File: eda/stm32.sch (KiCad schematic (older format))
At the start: 28 parts

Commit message: refs #41563 refined em-lock schematics, 2 spi rc522 devices added.
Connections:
- net labels added: PB13_SPI2_SCK, PB14_SPI2_MISO, PB15_SPI2_MOSI, PB5_RC522A_CS, PB6_RC522B_CS, PB7_RC522_RST, PB8_RC522A_IRQ, PB9_RC522B_IRQ
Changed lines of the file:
@@
 Connection ~ 11950 4450
 Connection ~ 12350 4450
+Text HLabel 9350 3800 0    60   Input ~ 0
+PB13_SPI2_SCK
+Text HLabel 9350 3900 0    60   Input ~ 0
+PB14_SPI2_MISO
+Text HLabel 9350 4000 0    60   Input ~ 0
+PB15_SPI2_MOSI
+Text HLabel 9350 3300 0    60   Input ~ 0
+PB8_RC522A_IRQ
+Text HLabel 9350 3400 0    60   Input ~ 0
+PB9_RC522B_IRQ
+Text HLabel 9350 3200 0    60   Input ~ 0
+PB7_RC522_RST
+Text HLabel 9350 3000 0    60   Input ~ 0
+PB5_RC522A_CS
+Text HLabel 9350 3100 0    60   Input ~ 0
+PB6_RC522B_CS
 $EndSCHEMATC

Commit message: refs #41563 fix stable schematics version
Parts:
- added R29: 0, I20:R_0805, symbol R
- C10, C11, C12, C13, C14, C15, C16, C17, C18, C19, C20, C9: renamed from C?; footprint I20:C_0805_HandSoldering -> I20:C_0805
- D4: renamed from D?; footprint I20:Fuse_SMD1206_Wave -> Diodes_ThroughHole:Diode_DO-201AD_Horizontal_RM15
- SW1: renamed from SW?; footprint I20:SW_SPST_B3U-1000P -> I20:smd_push
- gave numbers to parts that had none: 14
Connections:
- wire segments 74 -> 72
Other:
- moved on the sheet: C11, C12, CON1, D4, F1, P12, P8, P9, U2

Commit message: refs #41563 pcb projecting half-done
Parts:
- removed P11: USB_B, I20:conn_usb_B_micro_smd-2, symbol USB_B
- F1: value F_Small -> 3A
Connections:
- net labels removed: +5V
- wire segments 72 -> 70
- no-connect marks 0 -> 1
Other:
- note removed: "USB power connector"
- moved on the sheet: P12
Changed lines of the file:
@@
-$EndComp
-$Comp
-L +5V #PWR040
-U 1 1 581973D6
-P 3700 4250
-F 0 "#PWR040" H 3700 4100 50  0001 C CNN
-F 1 "+5V" H 3700 4400 50  0000 C CNN
-F 2 "" H 3700 4250 50  0000 C CNN
-F 3 "" H 3700 4250 50  0000 C CNN
-	1    3700 4250
-	-1   0    0    1
 $EndComp
 $Comp
@@
 U 1 1 581973D8
 P 3900 4250
-F 0 "F1" V 3900 4050 50  0000 C CNN
-F 1 "F_Small" V 3800 4050 50  0000 C CNN
+F 0 "F1" V 3900 4100 50  0000 C CNN
+F 1 "3A" V 3800 4100 50  0000 C CNN
 F 2 "I20:Fuse_SMD1206_Wave" H 3900 4250 50  0001 C CNN
 F 3 "" H 3900 4250 50  0000 C CNN
@@
 Power connector
 Text Notes 8400 8400 0    60   ~ 0
-USB power connector
-Text Notes 12350 8400 0    60   ~ 0
 Serial debug connector
 $Comp
@@
 L CONN_01X04 P12
 U 1 1 581D0598
-P 13500 9190
-F 0 "P12" H 13419 8815 50  0000 C CNN
-F 1 "SWD_CONN" H 13419 8906 50  0000 C CNN
-F 2 "I20:Pin_Header_Straight_1x04" H 13500 9190 50  0001 C CNN
-F 3 "" H 13500 9190 50  0000 C CNN
-	1    13500 9190
+P 9650 9740
+F 0 "P12" H 9569 9365 50  0000 C CNN
+F 1 "SWD_CONN" H 9569 9456 50  0000 C CNN
+F 2 "I20:Pin_Header_Straight_1x04" H 9650 9740 50  0001 C CNN
+F 3 "" H 9650 9740 50  0000 C CNN
+	1    9650 9740
 	-1   0    0    1
 $EndComp
 $Comp
-L GND #PWR041
+L GND #PWR040
 U 1 1 581BD405
-P 13800 9040
-F 0 "#PWR041" H 13800 8790 50  0001 C CNN
-F 1 "GND" H 13805 8867 50  0000 C CNN
-F 2 "" H 13800 9040 50  0000 C CNN
-F 3 "" H 13800 9040 50  0000 C CNN
-	1    13800 9040
+P 9950 9590
+F 0 "#PWR040" H 9950 9340 50  0001 C CNN
+F 1 "GND" H 9955 9417 50  0000 C CNN
+F 2 "" H 9950 9590 50  0000 C CNN
+F 3 "" H 9950 9590 50  0000 C CNN
+	1    9950 9590
 	0    -1   -1   0
 $EndComp
 $Comp
-L VDD #PWR042
+L VDD #PWR041
 U 1 1 581BD6DF
-P 13800 9340
-F 0 "#PWR042" H 13800 9190 50  0001 C CNN
-F 1 "VDD" H 13817 9513 50  0000 C CNN
-F 2 "" H 13800 9340 50  0000 C CNN
-F 3 "" H 13800 9340 50  0000 C CNN
-	1    13800 9340
+P 9950 9890
+F 0 "#PWR041" H 9950 9740 50  0001 C CNN
+F 1 "VDD" H 9967 10063 50  0000 C CNN
+F 2 "" H 9950 9890 50  0000 C CNN
+F 3 "" H 9950 9890 50  0000 C CNN
+	1    9950 9890
 	0    1    1    0
 $EndComp
-Text Label 14050 9240 0    60   ~ 0
+Text Label 10200 9790 0    60   ~ 0
 SWDIO
-Text Label 14050 9140 0    60   ~ 0
+Text Label 10200 9690 0    60   ~ 0
 SWCLK
 Text Label 12500 7200 0    60   ~ 0
@@
 $EndComp
 $Comp
-L VCC #PWR043
+L VCC #PWR042
 U 1 1 581973DA
 P 5250 4750
-F 0 "#PWR043" H 5250 4600 50  0001 C CNN
+F 0 "#PWR042" H 5250 4600 50  0001 C CNN
 F 1 "VCC" H 5267 4923 50  0000 C CNN
 F 2 "" H 5250 4750 50  0000 C CNN
@@
 $EndComp
 $Comp
-L VDD #PWR044
+L VDD #PWR043
 U 1 1 57BEF7FC
 P 5050 4750
-F 0 "#PWR044" H 5050 4600 50  0001 C CNN
+F 0 "#PWR043" H 5050 4600 50  0001 C CNN
 F 1 "VDD" H 5067 4923 50  0000 C CNN
 F 2 "" H 5050 4750 50  0000 C CNN
@@
 $EndComp
 $Comp
-L USB_B P11
-U 1 1 581973D0
-P 10150 9750
-F 0 "P11" V 10130 9937 50  0000 L CNN
-F 1 "USB_B" V 10221 9937 50  0000 L CNN
-F 2 "I20:conn_usb_B_micro_smd-2" V 10100 9650 50  0001 C CNN
-F 3 "" V 10100 9650 50  0000 C CNN
-	1    10150 9750
-	0    1    1    0
-$EndComp
-$Comp
-L +5V #PWR045
-U 1 1 581973D3
-P 9750 9550
-F 0 "#PWR045" H 9750 9400 50  0001 C CNN
-F 1 "+5V" V 9850 9650 50  0000 C CNN
-F 2 "" H 9750 9550 50  0000 C CNN
-F 3 "" H 9750 9550 50  0000 C CNN
-	1    9750 9550
-	0    -1   -1   0
-$EndComp
-$Comp
-L GND #PWR046
-U 1 1 581973D1
-P 9750 9850
-F 0 "#PWR046" H 9750 9600 50  0001 C CNN
-F 1 "GND" V 9650 9750 50  0000 C CNN
-F 2 "" H 9750 9850 50  0000 C CNN
-F 3 "" H 9750 9850 50  0000 C CNN
-	1    9750 9850
-	0    1    1    0
-$EndComp
-$Comp
 L R R28
 U 1 1 581973B7
@@
 	0    1    1    0
 $EndComp
-Text HLabel 15150 2600 2    60   Input ~ 0
+Text HLabel 15150 2600 2    60   Output ~ 0
 PIN_RED
-Text HLabel 15150 2700 2    60   Input ~ 0
+Text HLabel 15150 2700 2    60   Output ~ 0
 PIN_GREEN
-Text HLabel 15150 2800 2    60   Input ~ 0
+Text HLabel 15150 2800 2    60   Output ~ 0
 PIN_BLUE
-Text HLabel 15150 3300 2    60   Input ~ 0
+Text HLabel 15150 3300 2    60   Output ~ 0
 ESP_RESET
 Text HLabel 15150 3500 2    60   Input ~ 0
 UART_INT_RX
-Text HLabel 15150 3400 2    60   Input ~ 0
+Text HLabel 15150 3400 2    60   Output ~ 0
 UART_INT_TX
 Text Label 15150 3800 0    60   ~ 0
@@
 SWCLK
 $Comp
-L GND #PWR047
+L GND #PWR044
 U 1 1 57BDD879
 P 12400 4450
-F 0 "#PWR047" H 12400 4200 50  0001 C CNN
+F 0 "#PWR044" H 12400 4200 50  0001 C CNN
 F 1 "GND" H 12405 4277 50  0000 C CNN
 F 2 "" H 12400 4450 50  0000 C CNN
@@
 Text HLabel 9350 3600 0    60   Input ~ 0
 UART_EXT_RX
-Text HLabel 9350 3500 0    60   Input ~ 0
+Text HLabel 9350 3500 0    60   Output ~ 0
 UART_EXT_TX
-Text HLabel 9350 2800 0    60   Input ~ 0
+Text HLabel 9350 2800 0    60   Output ~ 0
 LOCK_OPEN
-Text HLabel 9350 2700 0    60   Input ~ 0
-PB2/BOOT1
 Text HLabel 9350 2600 0    60   Input ~ 0
 BTN_CALL
 Text HLabel 9350 2500 0    60   Input ~ 0
 BTN_OPEN
+$Comp
+L STM32F103C8Tx U3
+U 1 1 581973DB
+P 12250 2600
+F 0 "U3" H 13050 3850 50  0000 C CNN
+F 1 "STM32F103C8Tx" H 13500 3850 50  0000 C CNN
+F 2 "I20:SparkFun-LQFP-48" H 13400 3700 50  0000 C CNN
+F 3 "" H 12250 2600 50  0000 C CNN
+	1    12250 2600
+	1    0    0    -1
+$EndComp
+Text HLabel 9350 3800 0    60   Output ~ 0
+PB13_SPI2_SCK
+Text HLabel 9350 3900 0    60   Input ~ 0
+PB14_SPI2_MISO
+Text HLabel 9350 4000 0    60   Output ~ 0
+PB15_SPI2_MOSI
+Text HLabel 9350 3300 0    60   Input ~ 0
+PB8_RC522A_IRQ
+Text HLabel 9350 3400 0    60   Input ~ 0
+PB9_RC522B_IRQ
+Text HLabel 9350 3200 0    60   Output ~ 0
+PB7_RC522_RST
+Text HLabel 9350 3000 0    60   Output ~ 0
+PB5_RC522A_CS
+Text HLabel 9350 3100 0    60   Output ~ 0
+PB6_RC522B_CS
+$Comp
+L R R29
+U 1 1 583D9C6F
+P 3900 4500
+F 0 "R29" V 3900 4450 50  0000 L CNN
+F 1 "0" H 4000 4500 50  0000 L CNN
+F 2 "I20:R_0805" V 3830 4500 50  0001 C CNN
+F 3 "" H 3900 4500 50  0000 C CNN
+	1    3900 4500
+	1    0    0    -1
+$EndComp
+Text Label 9350 2700 2    60   ~ 0
+PB2/BOOT1
 Wire Wire Line
 	5250 5000 5250 4750
@@
 	4400 5300 4400 5550
 Wire Wire Line
-	13800 9340 13700 9340
-Wire Wire Line
-	13800 9040 13700 9040
-Wire Wire Line
-	14050 9240 13700 9240
-Wire Wire Line
-	14050 9140 13700 9140
+	9950 9890 9850 9890
+Wire Wire Line
+	9950 9590 9850 9590
+Wire Wire Line
+	10200 9790 9850 9790
+Wire Wire Line
+	10200 9690 9850 9690
 Wire Notes Line
 	8270 480  8270 11215
@@
 Wire Notes Line
 	8270 8250 16060 8250
-Wire Notes Line
-	11800 9960 11800 8250
 Wire Wire Line
 	2450 1900 3100 1900
@@
 	12350 7600 12500 7600
 Wire Wire Line
-	9750 9550 9850 9550
-Wire Wire Line
-	9750 9850 9850 9850
-Wire Wire Line
 	4600 4100 4500 4100
 Wire Wire Line
@@
 	12350 750  12350 800
 Connection ~ 12250 750
-$Comp
-L STM32F103C8Tx U3
-U 1 1 581973DB
-P 12250 2600
-F 0 "U3" H 13050 3850 50  0000 C CNN
-F 1 "STM32F103C8Tx" H 13500 3850 50  0000 C CNN
-F 2 "I20:SparkFun-LQFP-48" H 13400 3700 50  0000 C CNN
-F 3 "" H 12250 2600 50  0000 C CNN
-	1    12250 2600
-	1    0    0    -1
-$EndComp
 Connection ~ 12050 4450
 Connection ~ 11950 4450
 Connection ~ 12350 4450
-Text HLabel 9350 3800 0    60   Input ~ 0
-PB13_SPI2_SCK
-Text HLabel 9350 3900 0    60   Input ~ 0
-PB14_SPI2_MISO
-Text HLabel 9350 4000 0    60   Input ~ 0
-PB15_SPI2_MOSI
-Text HLabel 9350 3300 0    60   Input ~ 0
-PB8_RC522A_IRQ
-Text HLabel 9350 3400 0    60   Input ~ 0
-PB9_RC522B_IRQ
-Text HLabel 9350 3200 0    60   Input ~ 0
-PB7_RC522_RST
-Text HLabel 9350 3000 0    60   Input ~ 0
-PB5_RC522A_CS
-Text HLabel 9350 3100 0    60   Input ~ 0
-PB6_RC522B_CS
-$Comp
-L R R29
-U 1 1 583D9C6F
-P 3900 4500
-F 0 "R29" V 3900 4450 50  0000 L CNN
-F 1 "0" H 4000 4500 50  0000 L CNN
-F 2 "I20:R_0805" V 3830 4500 50  0001 C CNN
-F 3 "" H 3900 4500 50  0000 C CNN
-	1    3900 4500
-	1    0    0    -1
-$EndComp
+NoConn ~ 3700 4250
 $EndSCHEMATC

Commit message: refs #41563 rc522 moved up, RGB LEDs moved to separate pcbs, 3d model of rc522 implemented.
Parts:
- removed P8: PWR_SELECT, I20:Pin_Header_Straight_1x03, symbol CONN_01X03
- D4: footprint Diodes_ThroughHole:Diode_DO-201AD_Horizontal_RM15 -> I20:MiniMELF_Standard
- D5: renamed from R29; footprint I20:R_0805 -> I20:Diode_DO-201AD_Horizontal_RM15; symbol R -> D
- SW1: footprint I20:smd_push -> I20:PCB_PUSH
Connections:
- net 12V_EXT: now also F1.2
- net at F1.1: now also D5.2 (A); no longer D5.1
- net at P9.2 (P2): now also D5.1 (K); no longer D5.2
- no-connect marks 1 -> 0
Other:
- moved on the sheet: F1
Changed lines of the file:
@@
 $EndDescr
 $Comp
-L VDD #PWR032
+L VDD #PWR033
 U 1 1 57BED091
 P 12050 750
-F 0 "#PWR032" H 12050 600 50  0001 C CNN
+F 0 "#PWR033" H 12050 600 50  0001 C CNN
 F 1 "VDD" V 12100 700 50  0000 C CNN
 F 2 "" H 12050 750 50  0000 C CNN
@@
 $EndComp
 $Comp
-L GND #PWR033
+L GND #PWR034
 U 1 1 57BED7A6
 P 2000 1900
-F 0 "#PWR033" H 2000 1650 50  0001 C CNN
+F 0 "#PWR034" H 2000 1650 50  0001 C CNN
 F 1 "GND" H 2005 1727 50  0000 C CNN
 F 2 "" H 2000 1900 50  0000 C CNN
@@
 $EndComp
 $Comp
-L GND #PWR034
+L GND #PWR035
 U 1 1 581973BA
 P 11200 7400
-F 0 "#PWR034" H 11200 7150 50  0001 C CNN
+F 0 "#PWR035" H 11200 7150 50  0001 C CNN
 F 1 "GND" H 11205 7227 50  0000 C CNN
 F 2 "" H 11200 7400 50  0000 C CNN
@@
 $EndComp
 $Comp
-L VDD #PWR035
+L VDD #PWR036
 U 1 1 581973C3
 P 2700 2300
-F 0 "#PWR035" H 2700 2150 50  0001 C CNN
+F 0 "#PWR036" H 2700 2150 50  0001 C CNN
 F 1 "VDD" H 2717 2473 50  0000 C CNN
 F 2 "" H 2700 2300 50  0000 C CNN
@@
 $EndComp
 $Comp
-L GND #PWR036
+L GND #PWR037
 U 1 1 581973C9
 P 6150 2250
-F 0 "#PWR036" H 6150 2000 50  0001 C CNN
+F 0 "#PWR037" H 6150 2000 50  0001 C CNN
 F 1 "GND" H 6155 2077 50  0000 C CNN
 F 2 "" H 6150 2250 50  0000 C CNN
@@
 $EndComp
 $Comp
-L VDD #PWR037
+L VDD #PWR038
 U 1 1 581973CA
 P 6150 1550
-F 0 "#PWR037" H 6150 1400 50  0001 C CNN
+F 0 "#PWR038" H 6150 1400 50  0001 C CNN
 F 1 "VDD" H 6167 1723 50  0000 C CNN
 F 2 "" H 6150 1550 50  0000 C CNN
@@
 $EndComp
 $Comp
-L GND #PWR038
+L GND #PWR039
 U 1 1 581973CC
 P 4400 5550
-F 0 "#PWR038" H 4400 5300 50  0001 C CNN
+F 0 "#PWR039" H 4400 5300 50  0001 C CNN
 F 1 "GND" H 4405 5377 50  0000 C CNN
 F 2 "" H 4400 5550 50  0000 C CNN
@@
 F 0 "D4" V 3404 5329 50  0000 L CNN
 F 1 "LDO-12V" H 3250 5150 50  0000 L CNN
-F 2 "Diodes_ThroughHole:Diode_DO-201AD_Horizontal_RM15" H 3450 5250 50  0001 C CNN
+F 2 "I20:MiniMELF_Standard" H 3450 5250 50  0001 C CNN
 F 3 "" H 3450 5250 50  0000 C CNN
 	1    3450 5250
@@
 $EndComp
 $Comp
-L GND #PWR039
+L GND #PWR040
 U 1 1 581973D5
 P 4400 4000
-F 0 "#PWR039" H 4400 3750 50  0001 C CNN
+F 0 "#PWR040" H 4400 3750 50  0001 C CNN
 F 1 "GND" V 4300 3800 50  0000 C CNN
 F 2 "" H 4400 4000 50  0000 C CNN
@@
 $EndComp
 $Comp
-L CONN_01X03 P8
-U 1 1 581973D7
-P 3500 4150
-F 0 "P8" H 3450 4500 50  0000 L CNN
-F 1 "PWR_SELECT" H 3100 4400 50  0000 L CNN
-F 2 "I20:Pin_Header_Straight_1x03" H 3500 4150 50  0001 C CNN
-F 3 "" H 3500 4150 50  0000 C CNN
-	1    3500 4150
-	-1   0    0    -1
-$EndComp
-$Comp
 L F_Small F1
 U 1 1 581973D8
-P 3900 4250
-F 0 "F1" V 3900 4100 50  0000 C CNN
-F 1 "3A" V 3800 4100 50  0000 C CNN
-F 2 "I20:Fuse_SMD1206_Wave" H 3900 4250 50  0001 C CNN
-F 3 "" H 3900 4250 50  0000 C CNN
-	1    3900 4250
-	0    -1   -1   0
+P 4000 4200
+F 0 "F1" H 4000 4385 50  0000 C CNN
+F 1 "3A" H 4000 4294 50  0000 C CNN
+F 2 "I20:Fuse_SMD1206_Wave" H 4000 4200 50  0001 C CNN
+F 3 "" H 4000 4200 50  0000 C CNN
+	1    4000 4200
+	1    0    0    -1
 $EndComp
 Text Label 4600 5500 0    60   ~ 0
@@
 F 0 "SW1" H 2300 1755 50  0000 C CNN
 F 1 "RST_BTN" H 2300 1664 50  0000 C CNN
-F 2 "I20:smd_push" H 2300 1500 50  0001 C CNN
+F 2 "I20:PCB_PUSH" H 2300 1500 50  0001 C CNN
 F 3 "" H 2300 1500 50  0000 C CNN
 	1    2300 1500
@@
 $EndComp
 $Comp
-L GND #PWR040
+L GND #PWR041
 U 1 1 581BD405
 P 9950 9590
-F 0 "#PWR040" H 9950 9340 50  0001 C CNN
+F 0 "#PWR041" H 9950 9340 50  0001 C CNN
 F 1 "GND" H 9955 9417 50  0000 C CNN
 F 2 "" H 9950 9590 50  0000 C CNN
@@
 $EndComp
 $Comp
-L VDD #PWR041
+L VDD #PWR042
 U 1 1 581BD6DF
 P 9950 9890
-F 0 "#PWR041" H 9950 9740 50  0001 C CNN
+F 0 "#PWR042" H 9950 9740 50  0001 C CNN
 F 1 "VDD" H 9967 10063 50  0000 C CNN
 F 2 "" H 9950 9890 50  0000 C CNN
@@
 $EndComp
 $Comp
-L VCC #PWR042
+L VCC #PWR043
 U 1 1 581973DA
 P 5250 4750
-F 0 "#PWR042" H 5250 4600 50  0001 C CNN
+F 0 "#PWR043" H 5250 4600 50  0001 C CNN
 F 1 "VCC" H 5267 4923 50  0000 C CNN
 F 2 "" H 5250 4750 50  0000 C CNN
@@
 $EndComp
 $Comp
-L VDD #PWR043
+L VDD #PWR044
 U 1 1 57BEF7FC
 P 5050 4750
-F 0 "#PWR043" H 5050 4600 50  0001 C CNN
+F 0 "#PWR044" H 5050 4600 50  0001 C CNN
 F 1 "VDD" H 5067 4923 50  0000 C CNN
 F 2 "" H 5050 4750 50  0000 C CNN
@@
 SWCLK
 $Comp
-L GND #PWR044
+L GND #PWR045
 U 1 1 57BDD879
 P 12400 4450
-F 0 "#PWR044" H 12400 4200 50  0001 C CNN
+F 0 "#PWR045" H 12400 4200 50  0001 C CNN
 F 1 "GND" H 12405 4277 50  0000 C CNN
 F 2 "" H 12400 4450 50  0000 C CNN
@@
 PB6_RC522B_CS
 $Comp
-L R R29
+L D D5
 U 1 1 583D9C6F
-P 3900 4500
-F 0 "R29" V 3900 4450 50  0000 L CNN
-F 1 "0" H 4000 4500 50  0000 L CNN
-F 2 "I20:R_0805" V 3830 4500 50  0001 C CNN
-F 3 "" H 3900 4500 50  0000 C CNN
-	1    3900 4500
-	1    0    0    -1
+P 3900 4450
+F 0 "D5" V 3946 4372 50  0000 R CNN
+F 1 "0" V 3855 4372 50  0000 R CNN
+F 2 "I20:Diode_DO-201AD_Horizontal_RM15" V 3830 4450 50  0001 C CNN
+F 3 "" H 3900 4450 50  0000 C CNN
+	1    3900 4450
+	0    -1   -1   0
 $EndComp
 Text Label 9350 2700 2    60   ~ 0
@@
 	4100 4200 4600 4200
 Wire Wire Line
-	4100 4050 4100 4200
-Wire Wire Line
 	4400 4000 4600 4000
 Wire Wire Line
@@
 Connection ~ 4500 4000
 Wire Wire Line
-	3700 4150 3900 4150
-Wire Wire Line
-	4100 4050 3700 4050
-Wire Wire Line
 	3700 4750 3750 4750
-Wire Wire Line
-	3700 4650 3900 4650
 Wire Wire Line
 	12050 800  12050 750
@@
 Connection ~ 11950 4450
 Connection ~ 12350 4450
-NoConn ~ 3700 4250
+Wire Wire Line
+	3900 4200 3900 4300
+Wire Wire Line
+	3700 4650 3900 4650
+Wire Wire Line
+	3900 4650 3900 4600
 $EndSCHEMATC

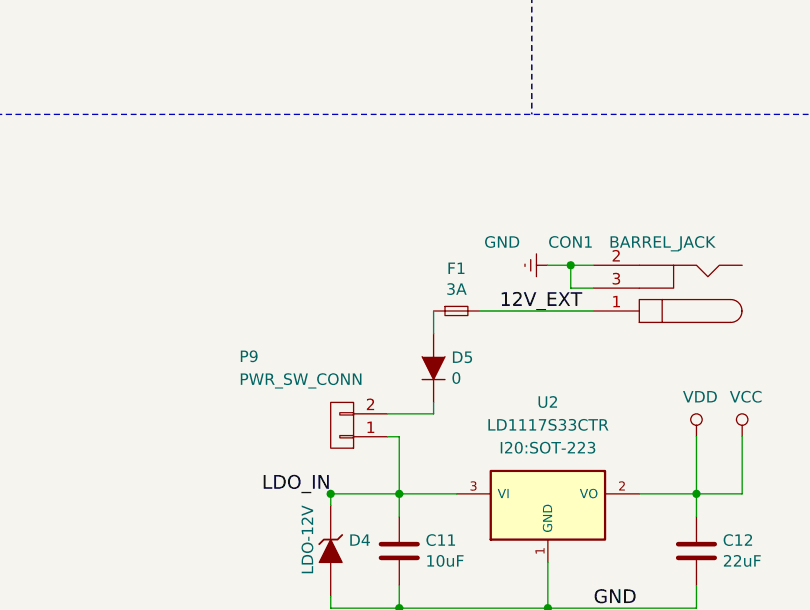
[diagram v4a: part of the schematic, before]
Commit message: refs #41563 main pcb done, todo: leds pcb multiplexor
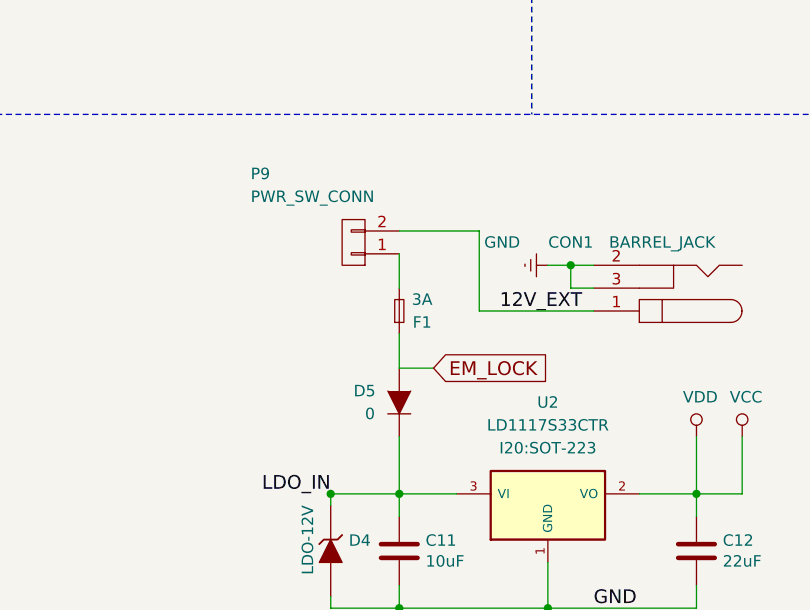
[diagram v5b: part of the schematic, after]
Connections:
- net 12V_EXT: now also P9.2 (P2); no longer F1.2
- net LDO_IN: now also D5.1 (K); no longer P9.1 (P1)
- net EM_LOCK: now reaches D5.2 (A), F1.1
- new net: F1.2, P9.1 (P1)
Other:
- moved on the sheet: D5, F1, P9
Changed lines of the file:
@@
 L F_Small F1
 U 1 1 581973D8
-P 4000 4200
-F 0 "F1" H 4000 4385 50  0000 C CNN
-F 1 "3A" H 4000 4294 50  0000 C CNN
-F 2 "I20:Fuse_SMD1206_Wave" H 4000 4200 50  0001 C CNN
-F 3 "" H 4000 4200 50  0000 C CNN
-	1    4000 4200
-	1    0    0    -1
+P 3750 4200
+F 0 "F1" V 3700 4100 50  0000 C CNN
+F 1 "3A" V 3800 4100 50  0000 C CNN
+F 2 "I20:Fuse_SMD1206_Wave" H 3750 4200 50  0001 C CNN
+F 3 "" H 3750 4200 50  0000 C CNN
+	1    3750 4200
+	0    -1   -1   0
 $EndComp
 Text Label 4600 5500 0    60   ~ 0
@@
 L CONN_01X02 P9
 U 1 1 581973D9
-P 3500 4700
-F 0 "P9" H 3950 4400 50  0000 R CNN
-F 1 "PWR_SW_CONN" H 3950 4500 50  0000 R CNN
-F 2 "I20:JST_XH_B02B-XH-A_02x2.50mm_Straight" H 3500 4700 50  0001 C CNN
-F 3 "" H 3500 4700 50  0000 C CNN
-	1    3500 4700
+P 3550 3900
+F 0 "P9" H 4000 3600 50  0000 R CNN
+F 1 "PWR_SW_CONN" H 4000 3700 50  0000 R CNN
+F 2 "I20:JST_XH_B02B-XH-A_02x2.50mm_Straight" H 3550 3900 50  0001 C CNN
+F 3 "" H 3550 3900 50  0000 C CNN
+	1    3550 3900
 	-1   0    0    1
 $EndComp
@@
 L D D5
 U 1 1 583D9C6F
-P 3900 4450
-F 0 "D5" V 3946 4372 50  0000 R CNN
-F 1 "0" V 3855 4372 50  0000 R CNN
-F 2 "I20:Diode_DO-201AD_Horizontal_RM15" V 3830 4450 50  0001 C CNN
-F 3 "" H 3900 4450 50  0000 C CNN
-	1    3900 4450
+P 3750 4600
+F 0 "D5" V 3800 4800 50  0000 R CNN
+F 1 "0" V 3700 4750 50  0000 R CNN
+F 2 "I20:Diode_DO-201AD_Horizontal_RM15" V 3680 4600 50  0001 C CNN
+F 3 "" H 3750 4600 50  0000 C CNN
+	1    3750 4600
 	0    -1   -1   0
 $EndComp
 Text Label 9350 2700 2    60   ~ 0
 PB2/BOOT1
+Text GLabel 3900 4450 2    60   Input ~ 0
+EM_LOCK
 Wire Wire Line
 	5250 5000 5250 4750
@@
 Connection ~ 4500 4000
 Wire Wire Line
-	3700 4750 3750 4750
-Wire Wire Line
 	12050 800  12050 750
 Wire Wire Line
@@
 Connection ~ 12350 4450
 Wire Wire Line
-	3900 4200 3900 4300
-Wire Wire Line
-	3700 4650 3900 4650
-Wire Wire Line
-	3900 4650 3900 4600
+	3900 4450 3750 4450
+Wire Wire Line
+	3750 4450 3750 4300
+Wire Wire Line
+	4100 4200 4100 3850
+Wire Wire Line
+	4100 3850 3750 3850
+Wire Wire Line
+	3750 3950 3750 4100
 $EndSCHEMATC
